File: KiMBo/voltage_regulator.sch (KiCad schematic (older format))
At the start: 12 parts, among them U4 RT8268

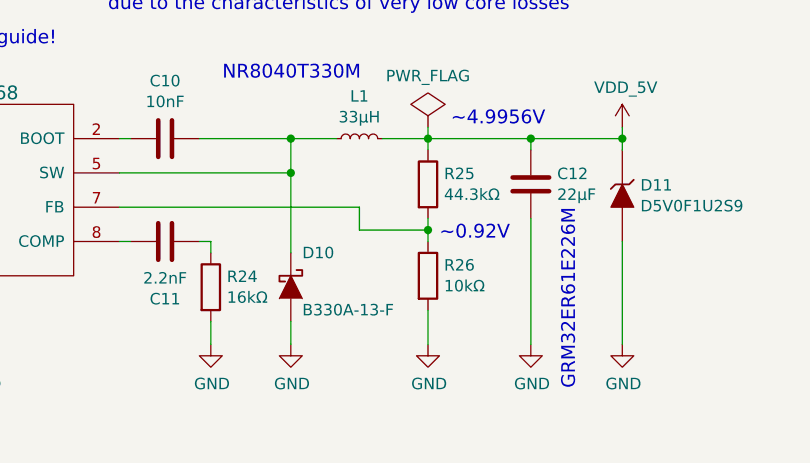
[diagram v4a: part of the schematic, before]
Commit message: Add equivalent annotations document, associate more footprints
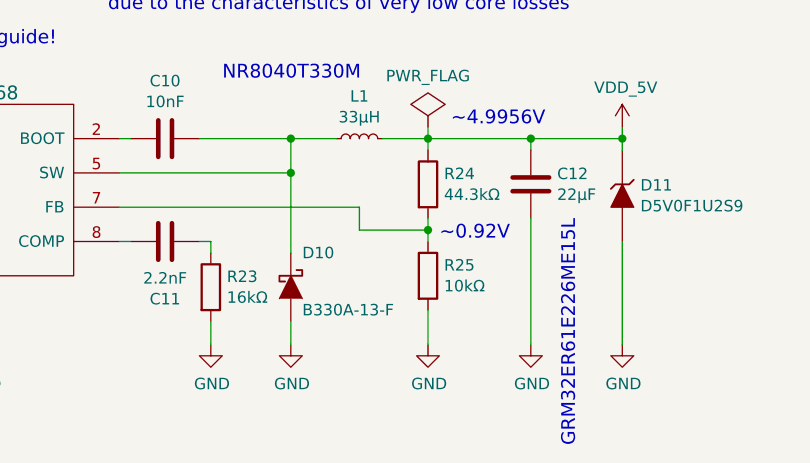
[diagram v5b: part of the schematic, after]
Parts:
- C10, C11, C9: footprint (none) -> Capacitors_SMD:C_0402
- C12: footprint (none) -> Capacitors_SMD:C_1210
- C8: footprint (none) -> Capacitors_SMD:C_1206
- renumbered R24 to R23, R25 to R24, R26 to R25
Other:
- note added: "GRM32ER61E226ME15L"
- note removed: "GRM32ER61E226M"
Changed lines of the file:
@@
 $EndDescr
 $Comp
-L PWR_FLAG #FLG075
+L PWR_FLAG #FLG074
 U 1 1 578901B0
 P 9250 4200
-F 0 "#FLG075" H 9250 4295 50  0001 C CNN
+F 0 "#FLG074" H 9250 4295 50  0001 C CNN
 F 1 "PWR_FLAG" H 9250 4424 50  0000 C CNN
 F 2 "" H 9250 4200 50  0000 C CNN
@@
 $EndComp
 $Comp
-L VDD_5V #PWR076
+L VDD_5V #PWR075
 U 1 1 59E9FFBE
 P 10100 4200
-F 0 "#PWR076" H 10100 4050 50  0001 C CNN
+F 0 "#PWR075" H 10100 4050 50  0001 C CNN
 F 1 "VDD_5V" H 10115 4373 50  0000 C CNN
 F 2 "" H 10100 4200 50  0000 C CNN
@@
 F 0 "C8" H 6265 4546 50  0000 L CNN
 F 1 "10μF" H 6265 4455 50  0000 L CNN
-F 2 "" H 6188 4350 50  0001 C CNN
+F 2 "Capacitors_SMD:C_1206" H 6188 4350 50  0001 C CNN
 F 3 "" H 6150 4500 50  0000 C CNN
 	1    6150 4500
@@
 	6700 4250 6150 4250
 $Comp
-L +24V #PWR077
+L +24V #PWR076
 U 1 1 59F3325A
 P 6150 4200
-F 0 "#PWR077" H 6150 4050 50  0001 C CNN
+F 0 "#PWR076" H 6150 4050 50  0001 C CNN
 F 1 "+24V" H 6165 4373 50  0000 C CNN
 F 2 "" H 6150 4200 50  0000 C CNN
@@
 F 0 "C9" H 6614 4796 50  0000 L CNN
 F 1 "10nF" H 6614 4705 50  0000 L CNN
-F 2 "" H 6538 4600 50  0001 C CNN
+F 2 "Capacitors_SMD:C_0402" H 6538 4600 50  0001 C CNN
 F 3 "" H 6500 4750 50  0000 C CNN
 	1    6500 4750
@@
 	7300 5050 7300 5150
 $Comp
-L GND #PWR078
+L GND #PWR077
 U 1 1 59F333D1
 P 7300 5150
-F 0 "#PWR078" H 7300 4900 50  0001 C CNN
+F 0 "#PWR077" H 7300 4900 50  0001 C CNN
 F 1 "GND" H 7305 4977 50  0000 C CNN
 F 2 "" H 7300 5150 50  0000 C CNN
@@
 F 0 "C10" V 7848 4250 50  0000 C CNN
 F 1 "10nF" V 7939 4250 50  0000 C CNN
-F 2 "" H 8138 4100 50  0001 C CNN
+F 2 "Capacitors_SMD:C_0402" H 8138 4100 50  0001 C CNN
 F 3 "" H 8100 4250 50  0000 C CNN
 	1    8100 4250
@@
 F 0 "C11" V 8352 4700 50  0000 C CNN
 F 1 "2.2nF" V 8261 4700 50  0000 C CNN
-F 2 "" H 8138 4550 50  0001 C CNN
+F 2 "Capacitors_SMD:C_0402" H 8138 4550 50  0001 C CNN
 F 3 "" H 8100 4700 50  0000 C CNN
 	1    8100 4700
@@
 $EndComp
 $Comp
-L R R24
+L R R23
 U 1 1 59F33FE9
 P 8300 4900
-F 0 "R24" H 8370 4946 50  0000 L CNN
+F 0 "R23" H 8370 4946 50  0000 L CNN
 F 1 "16kΩ" H 8370 4855 50  0000 L CNN
 F 2 "" V 8230 4900 50  0001 C CNN
@@
 	7950 4700 7900 4700
 $Comp
-L GND #PWR079
+L GND #PWR078
 U 1 1 59F340C2
 P 8300 5150
-F 0 "#PWR079" H 8300 4900 50  0001 C CNN
+F 0 "#PWR078" H 8300 4900 50  0001 C CNN
 F 1 "GND" H 8305 4977 50  0000 C CNN
 F 2 "" H 8300 5150 50  0000 C CNN
@@
 $EndComp
 $Comp
-L GND #PWR080
+L GND #PWR079
 U 1 1 59F340EC
 P 8650 5150
-F 0 "#PWR080" H 8650 4900 50  0001 C CNN
+F 0 "#PWR079" H 8650 4900 50  0001 C CNN
 F 1 "GND" H 8655 4977 50  0000 C CNN
 F 2 "" H 8650 5150 50  0000 C CNN
@@
 	8300 5150 8300 5050
 $Comp
-L R R25
+L R R24
 U 1 1 59F344C0
 P 9250 4450
-F 0 "R25" H 9320 4496 50  0000 L CNN
+F 0 "R24" H 9320 4496 50  0000 L CNN
 F 1 "44.3kΩ" H 9320 4405 50  0000 L CNN
 F 2 "" V 9180 4450 50  0001 C CNN
@@
 $EndComp
 $Comp
-L R R26
+L R R25
 U 1 1 59F344FF
 P 9250 4850
-F 0 "R26" H 9320 4896 50  0000 L CNN
+F 0 "R25" H 9320 4896 50  0000 L CNN
 F 1 "10kΩ" H 9320 4805 50  0000 L CNN
 F 2 "" V 9180 4850 50  0001 C CNN
@@
 F 0 "C12" H 9815 4496 50  0000 L CNN
 F 1 "22μF" H 9815 4405 50  0000 L CNN
-F 2 "" H 9738 4300 50  0001 C CNN
+F 2 "Capacitors_SMD:C_1210" H 9738 4300 50  0001 C CNN
 F 3 "" H 9700 4450 50  0000 C CNN
 	1    9700 4450
@@
 $EndComp
 $Comp
-L GND #PWR081
+L GND #PWR080
 U 1 1 59F34AA9
 P 9250 5150
-F 0 "#PWR081" H 9250 4900 50  0001 C CNN
+F 0 "#PWR080" H 9250 4900 50  0001 C CNN
 F 1 "GND" H 9255 4977 50  0000 C CNN
 F 2 "" H 9250 5150 50  0000 C CNN
@@
 	9700 4600 9700 5150
 $Comp
-L GND #PWR082
+L GND #PWR081
 U 1 1 59F34B40
 P 9700 5150
-F 0 "#PWR082" H 9700 4900 50  0001 C CNN
+F 0 "#PWR081" H 9700 4900 50  0001 C CNN
 F 1 "GND" H 9705 4977 50  0000 C CNN
 F 2 "" H 9700 5150 50  0000 C CNN
@@
 	6500 5100 7300 5100
 $Comp
-L GND #PWR083
+L GND #PWR082
 U 1 1 59F365D1
 P 6150 5150
-F 0 "#PWR083" H 6150 4900 50  0001 C CNN
+F 0 "#PWR082" H 6150 4900 50  0001 C CNN
 F 1 "GND" H 6155 4977 50  0000 C CNN
 F 2 "" H 6150 5150 50  0000 C CNN
@@
 	10100 4200 10100 4300
 $Comp
-L GND #PWR084
+L GND #PWR083
 U 1 1 5B79111A
 P 10100 5150
-F 0 "#PWR084" H 10100 4900 50  0001 C CNN
+F 0 "#PWR083" H 10100 4900 50  0001 C CNN
 F 1 "GND" H 10105 4977 50  0000 C CNN
 F 2 "" H 10100 5150 50  0000 C CNN
@@
 Wire Wire Line
 	9050 4250 10100 4250
-Text Notes 9900 5350 1    60   ~ 0
-GRM32ER61E226M
+Text Notes 9900 5600 1    60   ~ 0
+GRM32ER61E226ME15L
 Text Notes 8350 4000 0    60   ~ 0
 NR8040T330M

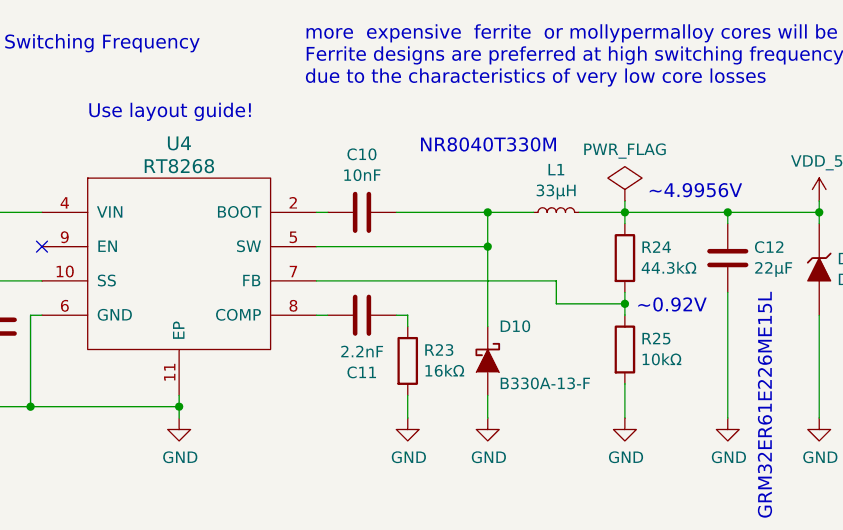
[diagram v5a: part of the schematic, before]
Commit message: Leave SPI0 free for a display, reassign pins so SPI1 is available
Fix some typos/errors
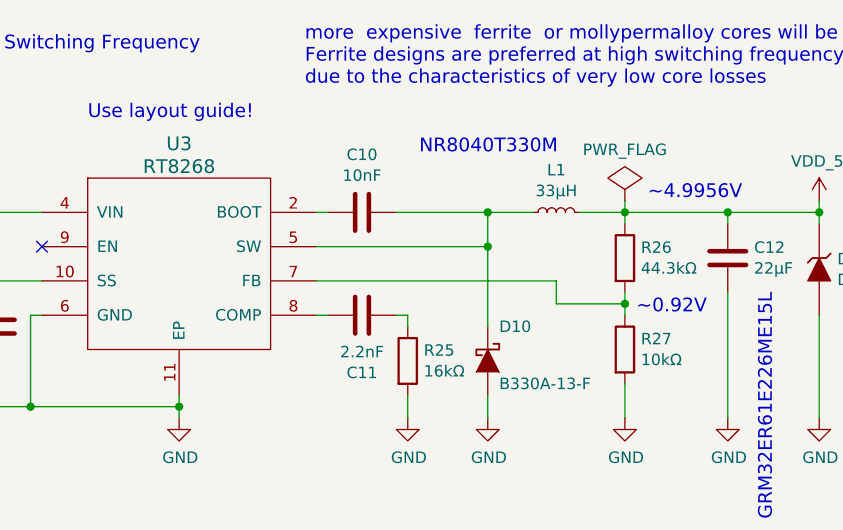
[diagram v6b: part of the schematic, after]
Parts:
- renumbered R23 to R25, R24 to R26, R25 to R27, U4 to U3
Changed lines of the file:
@@
 $EndDescr
 $Comp
-L PWR_FLAG #FLG074
+L PWR_FLAG #FLG073
 U 1 1 578901B0
 P 9250 4200
-F 0 "#FLG074" H 9250 4295 50  0001 C CNN
+F 0 "#FLG073" H 9250 4295 50  0001 C CNN
 F 1 "PWR_FLAG" H 9250 4424 50  0000 C CNN
 F 2 "" H 9250 4200 50  0000 C CNN
@@
 $EndComp
 $Comp
-L VDD_5V #PWR075
+L VDD_5V #PWR074
 U 1 1 59E9FFBE
 P 10100 4200
-F 0 "#PWR075" H 10100 4050 50  0001 C CNN
+F 0 "#PWR074" H 10100 4050 50  0001 C CNN
 F 1 "VDD_5V" H 10115 4373 50  0000 C CNN
 F 2 "" H 10100 4200 50  0000 C CNN
@@
 $EndComp
 $Comp
-L RT8268 U4
+L RT8268 U3
 U 1 1 59F30B79
 P 7300 4500
-F 0 "U4" H 7300 5050 60  0000 C CNN
+F 0 "U3" H 7300 5050 60  0000 C CNN
 F 1 "RT8268" H 7300 4950 60  0000 C CNN
 F 2 "" H 7300 4500 60  0001 C CNN
@@
 	6700 4250 6150 4250
 $Comp
-L +24V #PWR076
+L +24V #PWR075
 U 1 1 59F3325A
 P 6150 4200
-F 0 "#PWR076" H 6150 4050 50  0001 C CNN
+F 0 "#PWR075" H 6150 4050 50  0001 C CNN
 F 1 "+24V" H 6165 4373 50  0000 C CNN
 F 2 "" H 6150 4200 50  0000 C CNN
@@
 	7300 5050 7300 5150
 $Comp
-L GND #PWR077
+L GND #PWR076
 U 1 1 59F333D1
 P 7300 5150
-F 0 "#PWR077" H 7300 4900 50  0001 C CNN
+F 0 "#PWR076" H 7300 4900 50  0001 C CNN
 F 1 "GND" H 7305 4977 50  0000 C CNN
 F 2 "" H 7300 5150 50  0000 C CNN
@@
 $EndComp
 $Comp
-L R R23
+L R R25
 U 1 1 59F33FE9
 P 8300 4900
-F 0 "R23" H 8370 4946 50  0000 L CNN
+F 0 "R25" H 8370 4946 50  0000 L CNN
 F 1 "16kΩ" H 8370 4855 50  0000 L CNN
 F 2 "" V 8230 4900 50  0001 C CNN
@@
 	7950 4700 7900 4700
 $Comp
-L GND #PWR078
+L GND #PWR077
 U 1 1 59F340C2
 P 8300 5150
-F 0 "#PWR078" H 8300 4900 50  0001 C CNN
+F 0 "#PWR077" H 8300 4900 50  0001 C CNN
 F 1 "GND" H 8305 4977 50  0000 C CNN
 F 2 "" H 8300 5150 50  0000 C CNN
@@
 $EndComp
 $Comp
-L GND #PWR079
+L GND #PWR078
 U 1 1 59F340EC
 P 8650 5150
-F 0 "#PWR079" H 8650 4900 50  0001 C CNN
+F 0 "#PWR078" H 8650 4900 50  0001 C CNN
 F 1 "GND" H 8655 4977 50  0000 C CNN
 F 2 "" H 8650 5150 50  0000 C CNN
@@
 	8300 5150 8300 5050
 $Comp
-L R R24
+L R R26
 U 1 1 59F344C0
 P 9250 4450
-F 0 "R24" H 9320 4496 50  0000 L CNN
+F 0 "R26" H 9320 4496 50  0000 L CNN
 F 1 "44.3kΩ" H 9320 4405 50  0000 L CNN
 F 2 "" V 9180 4450 50  0001 C CNN
@@
 $EndComp
 $Comp
-L R R25
+L R R27
 U 1 1 59F344FF
 P 9250 4850
-F 0 "R25" H 9320 4896 50  0000 L CNN
+F 0 "R27" H 9320 4896 50  0000 L CNN
 F 1 "10kΩ" H 9320 4805 50  0000 L CNN
 F 2 "" V 9180 4850 50  0001 C CNN
@@
 $EndComp
 $Comp
-L GND #PWR080
+L GND #PWR079
 U 1 1 59F34AA9
 P 9250 5150
-F 0 "#PWR080" H 9250 4900 50  0001 C CNN
+F 0 "#PWR079" H 9250 4900 50  0001 C CNN
 F 1 "GND" H 9255 4977 50  0000 C CNN
 F 2 "" H 9250 5150 50  0000 C CNN
@@
 	9700 4600 9700 5150
 $Comp
-L GND #PWR081
+L GND #PWR080
 U 1 1 59F34B40
 P 9700 5150
-F 0 "#PWR081" H 9700 4900 50  0001 C CNN
+F 0 "#PWR080" H 9700 4900 50  0001 C CNN
 F 1 "GND" H 9705 4977 50  0000 C CNN
 F 2 "" H 9700 5150 50  0000 C CNN
@@
 	6500 5100 7300 5100
 $Comp
-L GND #PWR082
+L GND #PWR081
 U 1 1 59F365D1
 P 6150 5150
-F 0 "#PWR082" H 6150 4900 50  0001 C CNN
+F 0 "#PWR081" H 6150 4900 50  0001 C CNN
 F 1 "GND" H 6155 4977 50  0000 C CNN
 F 2 "" H 6150 5150 50  0000 C CNN
@@
 	10100 4200 10100 4300
 $Comp
-L GND #PWR083
+L GND #PWR082
 U 1 1 5B79111A
 P 10100 5150
-F 0 "#PWR083" H 10100 4900 50  0001 C CNN
+F 0 "#PWR082" H 10100 4900 50  0001 C CNN
 F 1 "GND" H 10105 4977 50  0000 C CNN
 F 2 "" H 10100 5150 50  0000 C CNN

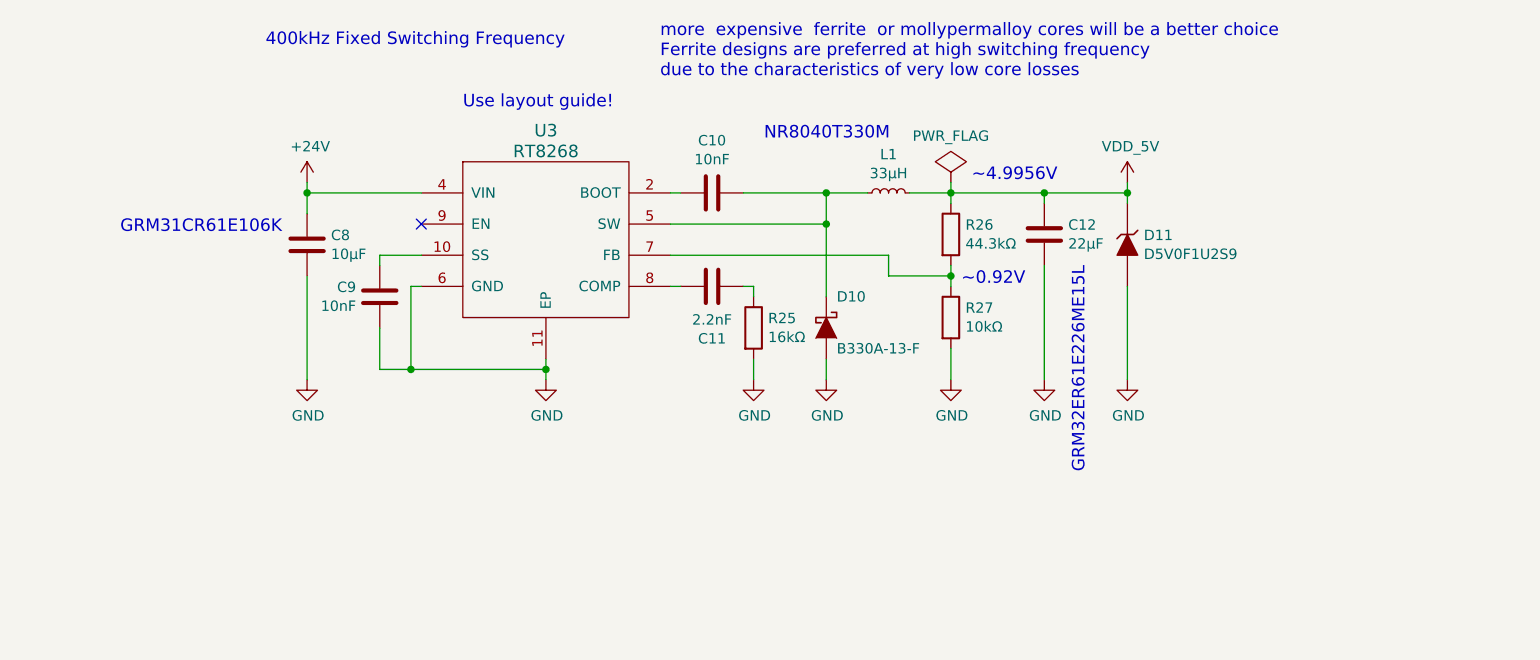
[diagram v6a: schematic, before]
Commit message: Use fixed 5V LM2592HV Buck, include SPI0 header for LCD
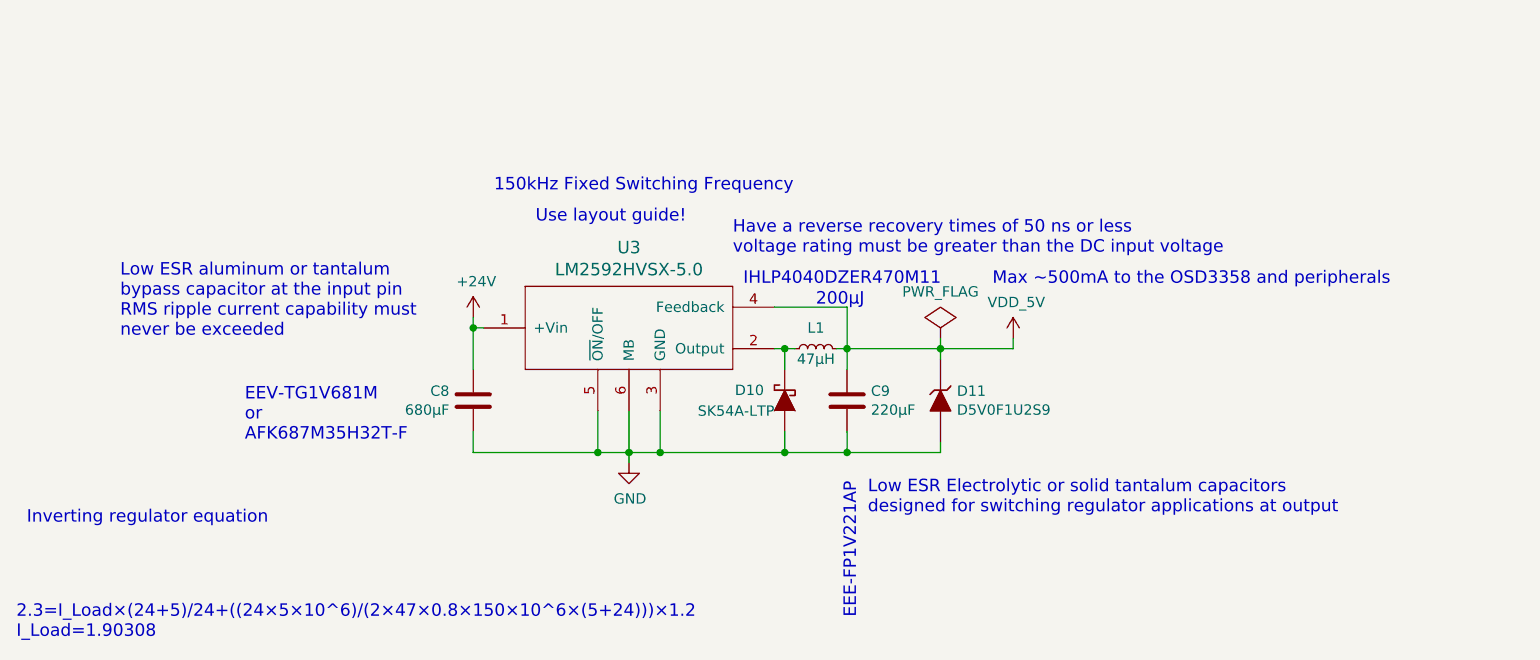
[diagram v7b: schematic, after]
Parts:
- removed C10, C9: 10nF, Capacitors_SMD:C_0402, symbol C
- removed C11: 2.2nF, Capacitors_SMD:C_0402, symbol C
- removed R25: 16kΩ, symbol R
- removed R26: 44.3kΩ, symbol R
- removed R27: 10kΩ, symbol R
- removed U3: RT8268, symbol RT8268
- added U3: LM2592HVSX-5.0, symbol LM2592HVSX-5.0
- C8: value 10μF -> 680μF
- C9: renamed from C12; value 22μF -> 220μF
- D10: value B330A-13-F -> SK54A-LTP
- L1: value 33μH -> 47μH
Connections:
- net +24V: now also U3.1 (+Vin)
- net GND: now also U3.3 (GND), U3.5 (~ON~/OFF), U3.6 (MB)
- net VDD_5V: now also U3.4 (Feedback)
- net at D10.1 (K), L1.1: now also U3.2 (Output)
- no-connect marks 1 -> 0
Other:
- note added: "150kHz Fixed Switching Frequency"
- note added: "2.3=I_Load×(24+5)/24+((24×5×10^6)/(2×47×0.8×150×10^6×(5+24)))×1.2\nI_Load=1.90308"
- note added: "200μJ"
- note added: "EEE-FP1V221AP"
- note added: "EEV-TG1V681M\nor\nAFK687M35H32T-F"
- note added: "Have a reverse recovery times of 50 ns or less\nvoltage rating must be greater than the DC input voltage"
- note added: "IHLP4040DZER470M11"
- note added: "Inverting regulator equation"
- note added: "Low ESR Electrolytic or solid tantalum capacitors\ndesigned for switching regulator applications at output"
- note added: "Low ESR aluminum or tantalum\nbypass capacitor at the input pin\nRMS ripple current capability must\nnever be exceeded"
- note added: "Max ~~500mA to the OSD3358 and peripherals"
- note removed: "400kHz Fixed Switching Frequency"
- note removed: "GRM31CR61E106K"
- note removed: "GRM32ER61E226ME15L"
- note removed: "NR8040T330M"
- note removed: "more expensive ferrite or mollypermalloy cores will be a better choice\nFerrite designs are preferred at high switching frequency\ndue to the characteristics of very low core losses"
- note removed: "~~0.92V"
- note removed: "~~4.9956V"
- moved on the sheet: C8, C9, D10, D11, L1

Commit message: Assocate more footprints
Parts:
- removed C8: 680μF, Capacitors_SMD:C_1206, symbol C
- removed C9: 220μF, Capacitors_SMD:C_1210, symbol C
- added C8: 470μF, symbol CP1
- added C9: 220μF, symbol CP1
- renumbered D10 to D11, D11 to D12
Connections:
- net +24V: now also C8.1
- net GND: now also C8.2, C9.2
- net VDD_5V: now also C9.1
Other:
- note added: "EEE-FK1H471AM\nor\nEEV-TG1V681M\nor\nAFK687M35H32T-F"
- note removed: "EEV-TG1V681M\nor\nAFK687M35H32T-F"
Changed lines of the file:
@@
-$EndComp
-$Comp
-L C C8
-U 1 1 59F33160
-P 6950 5250
-F 0 "C8" H 7065 5296 50  0000 L CNN
-F 1 "680μF" H 7065 5205 50  0000 L CNN
-F 2 "Capacitors_SMD:C_1206" H 6988 5100 50  0001 C CNN
-F 3 "" H 6950 5250 50  0000 C CNN
-	1    6950 5250
-	-1   0    0    -1
 $EndComp
 $Comp
@@
 	0    -1   -1   0
 $EndComp
-$Comp
-L C C9
-U 1 1 59F34902
-P 8750 5250
-F 0 "C9" H 8865 5296 50  0000 L CNN
-F 1 "220μF" H 8865 5205 50  0000 L CNN
-F 2 "Capacitors_SMD:C_1210" H 8788 5100 50  0001 C CNN
-F 3 "" H 8750 5250 50  0000 C CNN
-	1    8750 5250
-	1    0    0    -1
-$EndComp
 Text Notes 7250 4400 0    60   ~ 0
 Use layout guide!
 $Comp
-L ZENER D11
+L ZENER D12
 U 1 1 5B7841ED
 P 9200 5250
-F 0 "D11" V 9154 5329 50  0000 L CNN
+F 0 "D12" V 9154 5329 50  0000 L CNN
 F 1 "D5V0F1U2S9" V 9245 5329 50  0000 L CNN
 F 2 "" H 9200 5250 50  0001 C CNN
@@
 $EndComp
 $Comp
-L D_Schottky D10
+L D_Schottky D11
 U 1 1 5B78FD55
 P 8450 5250
-F 0 "D10" V 8400 5350 50  0000 L CNN
+F 0 "D11" V 8400 5350 50  0000 L CNN
 F 1 "SK54A-LTP" V 8500 5300 50  0000 L CNN
 F 2 "" H 8450 5250 50  0001 C CNN
@@
 Text Notes 8250 4700 0    60   ~ 0
 IHLP4040DZER470M11
-Text Notes 5850 5450 0    60   ~ 0
-EEV-TG1V681M\nor\nAFK687M35H32T-F
+Text Notes 5850 5500 0    60   ~ 0
+EEE-FK1H471AM\nor\nEEV-TG1V681M\nor\nAFK687M35H32T-F
 Text Notes 9450 4700 0    60   ~ 0
 Max ~~500mA to the OSD3358 and peripherals
@@
 Text Notes 4800 5850 0    60   ~ 0
 Inverting regulator equation
+$Comp
+L CP1 C8
+U 1 1 591FE1CF
+P 6950 5250
+F 0 "C8" H 7065 5296 50  0000 L CNN
+F 1 "470μF" H 7065 5205 50  0000 L CNN
+F 2 "" H 6950 5250 50  0001 C CNN
+F 3 "" H 6950 5250 50  0000 C CNN
+	1    6950 5250
+	-1   0    0    -1
+$EndComp
+$Comp
+L CP1 C9
+U 1 1 591FE334
+P 8750 5250
+F 0 "C9" H 8865 5296 50  0000 L CNN
+F 1 "220μF" H 8865 5205 50  0000 L CNN
+F 2 "" H 8750 5250 50  0001 C CNN
+F 3 "" H 8750 5250 50  0000 C CNN
+	1    8750 5250
+	1    0    0    -1
+$EndComp
 $EndSCHEMATC
